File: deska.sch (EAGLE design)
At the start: 23 parts, among them Q1 BC547, X1 JST-XH-03-PIN-LONG-PAD, X2 JST-XH-03-PIN-LONG-PAD, X3 JST-XH-03-PIN-LONG-PAD, X4 JST-XH-04-PIN-LONG-PAD, X5 JST-XH-04-PIN-LONG-PAD, X6 JST-XH-04-PIN-LONG-PAD, X7 JST-XH-03-PIN-LONG-PAD

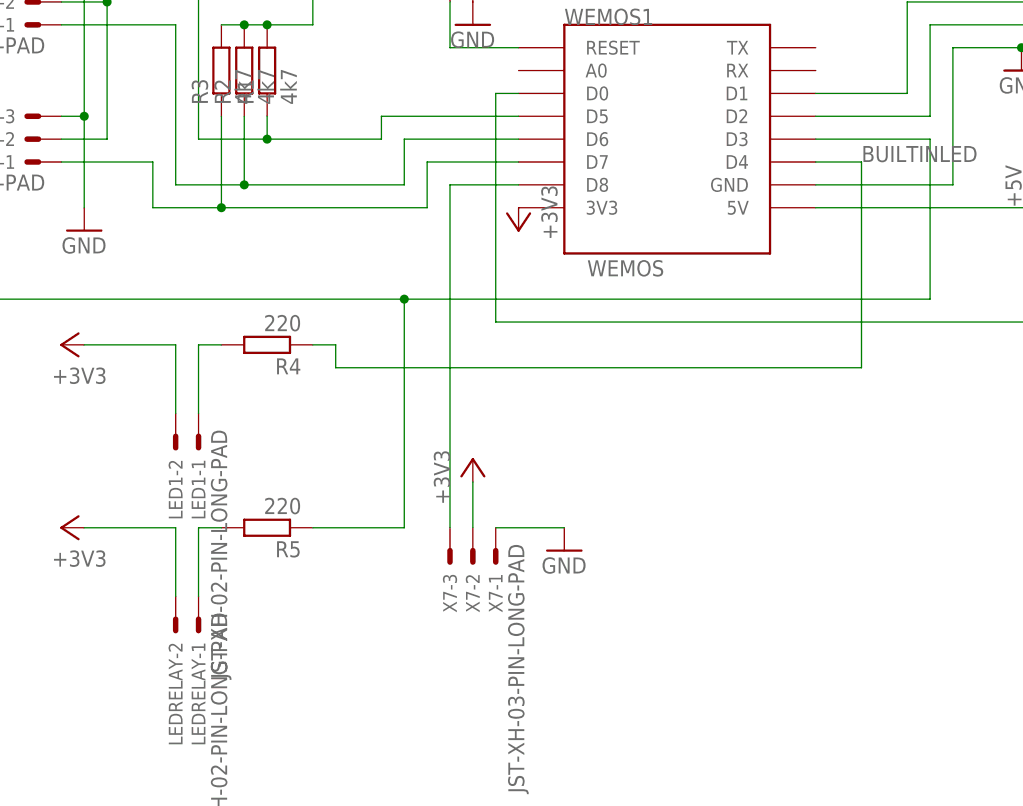
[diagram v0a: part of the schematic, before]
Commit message: deska s prohozením pinů
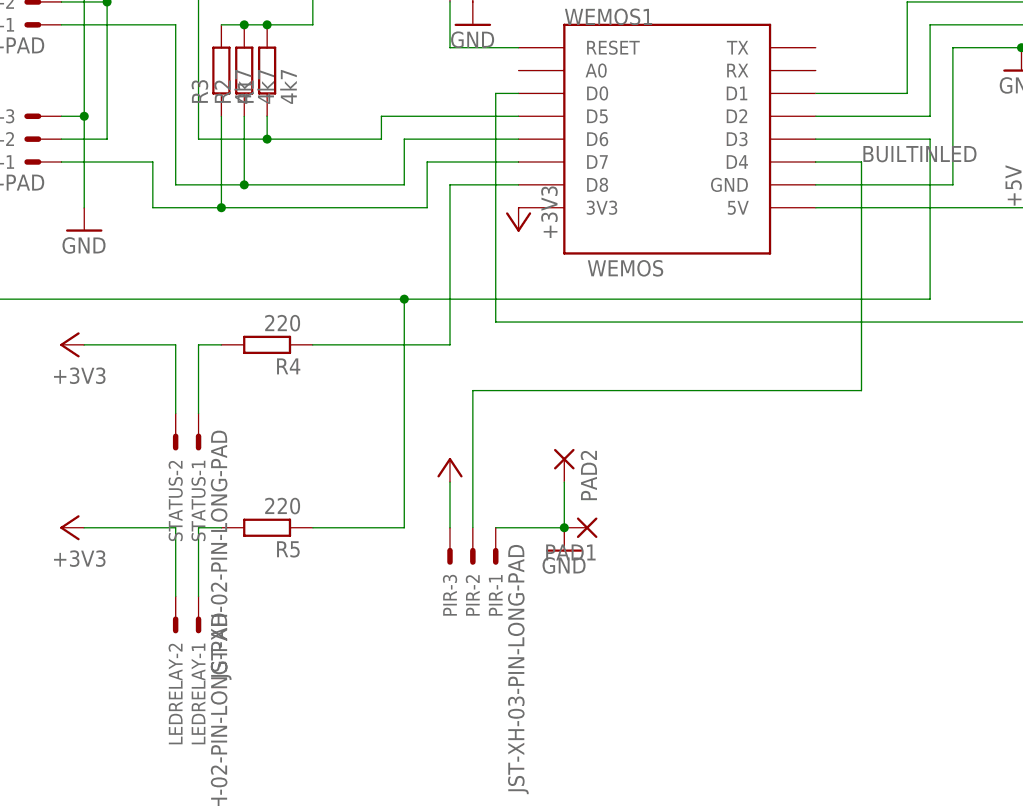
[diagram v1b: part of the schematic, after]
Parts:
- added PAD1, PAD2: (no value), wirepad:2,15/1,0
- renumbered LED1 to STATUS, X7 to PIR
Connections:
- net +3V3: now also PIR-3.S; no longer PIR-2.S
- net BUILTINLED: now also WEMOS1.D8; no longer WEMOS1.D4
- net GND: now also PAD1.P, PAD2.P
- net N$3: now also PIR-2.S, WEMOS1.D4; no longer PIR-3.S, WEMOS1.D8
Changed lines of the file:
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@@
 <part name="X6" library="Rembrandt Electronics - JST XH Connectors v1-0" deviceset="JST-XH-04-PIN" device="-LONG-PAD"/>
 <part name="RELAY" library="Rembrandt Electronics - JST XH Connectors v1-0" deviceset="JST-XH-03-PIN" device="-LONG-PAD"/>
-<part name="LED1" library="Rembrandt Electronics - JST XH Connectors v1-0" deviceset="JST-XH-02-PIN" device="-LONG-PAD"/>
+<part name="STATUS" library="Rembrandt Electronics - JST XH Connectors v1-0" deviceset="JST-XH-02-PIN" device="-LONG-PAD"/>
 <part name="LEDRELAY" library="Rembrandt Electronics - JST XH Connectors v1-0" deviceset="JST-XH-02-PIN" device="-LONG-PAD"/>
 <part name="BUZZER" library="Rembrandt Electronics - JST XH Connectors v1-0" deviceset="JST-XH-02-PIN" device="-LONG-PAD"/>
@@
 <part name="GND2" library="supply1" deviceset="GND" device=""/>
 <part name="+3V5" library="supply1" library_urn="urn:adsk.eagle:library:371" deviceset="+3V3" device=""/>
-<part name="X7" library="Rembrandt Electronics - JST XH Connectors v1-0" deviceset="JST-XH-03-PIN" device="-LONG-PAD"/>
+<part name="PIR" library="Rembrandt Electronics - JST XH Connectors v1-0" deviceset="JST-XH-03-PIN" device="-LONG-PAD"/>
 <part name="GND3" library="supply1" deviceset="GND" device=""/>
 <part name="RESET" library="Rembrandt Electronics - JST XH Connectors v1-0" deviceset="JST-XH-02-PIN" device="-LONG-PAD"/>
 <part name="GND7" library="supply1" deviceset="GND" device=""/>
+<part name="PAD1" library="wirepad" library_urn="urn:adsk.eagle:library:412" deviceset="2,15/1,0" device="" package3d_urn="urn:adsk.eagle:package:30831/1"/>
+<part name="PAD2" library="wirepad" library_urn="urn:adsk.eagle:library:412" deviceset="2,15/1,0" device="" package3d_urn="urn:adsk.eagle:package:30831/1"/>
 </parts>
 <sheets>
@@
 <attribute name="NAME" x="-33.02" y="56.642" size="1.524" layer="95" rot="R180"/>
 </instance>
-<instance part="LED1" gate="-2" x="10.16" y="27.94" smashed="yes" rot="R270">
+<instance part="STATUS" gate="-2" x="10.16" y="27.94" smashed="yes" rot="R270">
 <attribute name="NAME" x="9.398" y="25.4" size="1.524" layer="95" rot="R270"/>
 </instance>
-<instance part="LED1" gate="-1" x="12.7" y="27.94" smashed="yes" rot="R270">
+<instance part="STATUS" gate="-1" x="12.7" y="27.94" smashed="yes" rot="R270">
 <attribute name="NAME" x="11.938" y="25.4" size="1.524" layer="95" rot="R270"/>
 <attribute name="VALUE" x="14.097" y="28.702" size="1.778" layer="96" rot="R270"/>
@@
 <attribute name="VALUE" x="101.6" y="66.04" size="1.778" layer="96"/>
 </instance>
-<instance part="+3V5" gate="G$1" x="43.18" y="25.4" smashed="yes">
-<attribute name="VALUE" x="40.64" y="20.32" size="1.778" layer="96" rot="R90"/>
-</instance>
-<instance part="X7" gate="-1" x="45.72" y="15.24" smashed="yes" rot="R270">
+<instance part="+3V5" gate="G$1" x="40.64" y="25.4" smashed="yes"/>
+<instance part="PIR" gate="-1" x="45.72" y="15.24" smashed="yes" rot="R270">
 <attribute name="NAME" x="44.958" y="12.7" size="1.524" layer="95" rot="R270"/>
 <attribute name="VALUE" x="47.117" y="16.002" size="1.778" layer="96" rot="R270"/>
 </instance>
-<instance part="X7" gate="-2" x="43.18" y="15.24" smashed="yes" rot="R270">
+<instance part="PIR" gate="-2" x="43.18" y="15.24" smashed="yes" rot="R270">
 <attribute name="NAME" x="42.418" y="12.7" size="1.524" layer="95" rot="R270"/>
 </instance>
-<instance part="X7" gate="-3" x="40.64" y="15.24" smashed="yes" rot="R270">
+<instance part="PIR" gate="-3" x="40.64" y="15.24" smashed="yes" rot="R270">
 <attribute name="NAME" x="39.878" y="12.7" size="1.524" layer="95" rot="R270"/>
 </instance>
@@
 <instance part="GND7" gate="1" x="43.18" y="73.66" smashed="yes">
 <attribute name="VALUE" x="40.64" y="71.12" size="1.778" layer="96"/>
+</instance>
+<instance part="PAD1" gate="1" x="55.88" y="17.78" smashed="yes" rot="R180">
+<attribute name="NAME" x="57.023" y="15.9258" size="1.778" layer="95" rot="R180"/>
+<attribute name="VALUE" x="57.023" y="21.082" size="1.778" layer="96" rot="R180"/>
+</instance>
+<instance part="PAD2" gate="1" x="53.34" y="25.4" smashed="yes" rot="R270">
+<attribute name="NAME" x="55.1942" y="26.543" size="1.778" layer="95" rot="R270"/>
+<attribute name="VALUE" x="50.038" y="26.543" size="1.778" layer="96" rot="R270"/>
 </instance>
 </instances>
@@
 </segment>
 <segment>
-<pinref part="X7" gate="-1" pin="S"/>
 <pinref part="GND3" gate="1" pin="GND"/>
+<pinref part="PAD1" gate="1" pin="P"/>
+<pinref part="PIR" gate="-1" pin="S"/>
 <wire x1="45.72" y1="17.78" x2="53.34" y2="17.78" width="0.1524" layer="91"/>
+<junction x="53.34" y="17.78"/>
+<pinref part="PAD2" gate="1" pin="P"/>
+<wire x1="53.34" y1="22.86" x2="53.34" y2="17.78" width="0.1524" layer="91"/>
 </segment>
 <segment>
@@
 <pinref part="R4" gate="G$1" pin="2"/>
 <wire x1="12.7" y1="38.1" x2="15.24" y2="38.1" width="0.1524" layer="91"/>
-<pinref part="LED1" gate="-1" pin="S"/>
+<pinref part="STATUS" gate="-1" pin="S"/>
 <wire x1="12.7" y1="30.48" x2="12.7" y2="38.1" width="0.1524" layer="91"/>
 </segment>
@@
 <net name="BUILTINLED" class="0">
 <segment>
-<pinref part="WEMOS1" gate="D1" pin="D4"/>
-<wire x1="81.28" y1="58.42" x2="86.36" y2="58.42" width="0.1524" layer="91"/>
 <label x="86.36" y="58.42" size="1.778" layer="95"/>
-<wire x1="86.36" y1="58.42" x2="86.36" y2="35.56" width="0.1524" layer="91"/>
-<wire x1="27.94" y1="38.1" x2="25.4" y2="38.1" width="0.1524" layer="91"/>
 <pinref part="R4" gate="G$1" pin="1"/>
-<wire x1="86.36" y1="35.56" x2="27.94" y2="35.56" width="0.1524" layer="91"/>
-<wire x1="27.94" y1="35.56" x2="27.94" y2="38.1" width="0.1524" layer="91"/>
+<wire x1="25.4" y1="38.1" x2="40.64" y2="38.1" width="0.1524" layer="91"/>
+<wire x1="40.64" y1="38.1" x2="40.64" y2="55.88" width="0.1524" layer="91"/>
+<pinref part="WEMOS1" gate="D1" pin="D8"/>
+<wire x1="40.64" y1="55.88" x2="48.26" y2="55.88" width="0.1524" layer="91"/>
 </segment>
 </net>
@@
 <pinref part="+3V2" gate="G$1" pin="+3V3"/>
 <wire x1="10.16" y1="38.1" x2="0" y2="38.1" width="0.1524" layer="91"/>
-<pinref part="LED1" gate="-2" pin="S"/>
+<pinref part="STATUS" gate="-2" pin="S"/>
 <wire x1="10.16" y1="38.1" x2="10.16" y2="30.48" width="0.1524" layer="91"/>
 </segment>
@@
 </segment>
 <segment>
+<pinref part="PIR" gate="-3" pin="S"/>
 <pinref part="+3V5" gate="G$1" pin="+3V3"/>
-<wire x1="43.18" y1="22.86" x2="43.18" y2="17.78" width="0.1524" layer="91"/>
-<pinref part="X7" gate="-2" pin="S"/>
+<wire x1="40.64" y1="17.78" x2="40.64" y2="22.86" width="0.1524" layer="91"/>
 </segment>
 </net>
@@
 </segment>
 </net>
-<net name="N$3" class="0">
-<segment>
-<pinref part="WEMOS1" gate="D1" pin="D8"/>
-<wire x1="48.26" y1="55.88" x2="40.64" y2="55.88" width="0.1524" layer="91"/>
-<wire x1="40.64" y1="17.78" x2="40.64" y2="55.88" width="0.1524" layer="91"/>
-<pinref part="X7" gate="-3" pin="S"/>
-</segment>
-</net>
 <net name="N$5" class="0">
 <segment>
@@
 </segment>
 </net>
+<net name="N$3" class="0">
+<segment>
+<wire x1="43.18" y1="33.02" x2="86.36" y2="33.02" width="0.1524" layer="91"/>
+<wire x1="86.36" y1="33.02" x2="86.36" y2="58.42" width="0.1524" layer="91"/>
+<pinref part="WEMOS1" gate="D1" pin="D4"/>
+<wire x1="86.36" y1="58.42" x2="81.28" y2="58.42" width="0.1524" layer="91"/>
+<pinref part="PIR" gate="-2" pin="S"/>
+<wire x1="43.18" y1="17.78" x2="43.18" y2="33.02" width="0.1524" layer="91"/>
+</segment>
+</net>

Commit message: +
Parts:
- removed PAD1, PAD2: (no value), wirepad:2,15/1,0
- renumbered PIR to X7, STATUS to LED1
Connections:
- net +3V3: now also X7-2.S; no longer X7-3.S
- net BUILTINLED: now also WEMOS1.D4; no longer WEMOS1.D8
- net GND: no longer PAD1.P, PAD2.P
- net N$3: now also WEMOS1.D8, X7-3.S; no longer WEMOS1.D4, X7-2.S
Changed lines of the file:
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@@
 <part name="X6" library="Rembrandt Electronics - JST XH Connectors v1-0" deviceset="JST-XH-04-PIN" device="-LONG-PAD"/>
 <part name="RELAY" library="Rembrandt Electronics - JST XH Connectors v1-0" deviceset="JST-XH-03-PIN" device="-LONG-PAD"/>
-<part name="STATUS" library="Rembrandt Electronics - JST XH Connectors v1-0" deviceset="JST-XH-02-PIN" device="-LONG-PAD"/>
+<part name="LED1" library="Rembrandt Electronics - JST XH Connectors v1-0" deviceset="JST-XH-02-PIN" device="-LONG-PAD"/>
 <part name="LEDRELAY" library="Rembrandt Electronics - JST XH Connectors v1-0" deviceset="JST-XH-02-PIN" device="-LONG-PAD"/>
 <part name="BUZZER" library="Rembrandt Electronics - JST XH Connectors v1-0" deviceset="JST-XH-02-PIN" device="-LONG-PAD"/>
@@
 <part name="GND2" library="supply1" deviceset="GND" device=""/>
 <part name="+3V5" library="supply1" library_urn="urn:adsk.eagle:library:371" deviceset="+3V3" device=""/>
-<part name="PIR" library="Rembrandt Electronics - JST XH Connectors v1-0" deviceset="JST-XH-03-PIN" device="-LONG-PAD"/>
+<part name="X7" library="Rembrandt Electronics - JST XH Connectors v1-0" deviceset="JST-XH-03-PIN" device="-LONG-PAD"/>
 <part name="GND3" library="supply1" deviceset="GND" device=""/>
 <part name="RESET" library="Rembrandt Electronics - JST XH Connectors v1-0" deviceset="JST-XH-02-PIN" device="-LONG-PAD"/>
 <part name="GND7" library="supply1" deviceset="GND" device=""/>
-<part name="PAD1" library="wirepad" library_urn="urn:adsk.eagle:library:412" deviceset="2,15/1,0" device="" package3d_urn="urn:adsk.eagle:package:30831/1"/>
-<part name="PAD2" library="wirepad" library_urn="urn:adsk.eagle:library:412" deviceset="2,15/1,0" device="" package3d_urn="urn:adsk.eagle:package:30831/1"/>
 </parts>
 <sheets>
@@
 <attribute name="NAME" x="-33.02" y="56.642" size="1.524" layer="95" rot="R180"/>
 </instance>
-<instance part="STATUS" gate="-2" x="10.16" y="27.94" smashed="yes" rot="R270">
+<instance part="LED1" gate="-2" x="10.16" y="27.94" smashed="yes" rot="R270">
 <attribute name="NAME" x="9.398" y="25.4" size="1.524" layer="95" rot="R270"/>
 </instance>
-<instance part="STATUS" gate="-1" x="12.7" y="27.94" smashed="yes" rot="R270">
+<instance part="LED1" gate="-1" x="12.7" y="27.94" smashed="yes" rot="R270">
 <attribute name="NAME" x="11.938" y="25.4" size="1.524" layer="95" rot="R270"/>
 <attribute name="VALUE" x="14.097" y="28.702" size="1.778" layer="96" rot="R270"/>
@@
 <attribute name="VALUE" x="101.6" y="66.04" size="1.778" layer="96"/>
 </instance>
-<instance part="+3V5" gate="G$1" x="40.64" y="25.4" smashed="yes"/>
-<instance part="PIR" gate="-1" x="45.72" y="15.24" smashed="yes" rot="R270">
+<instance part="+3V5" gate="G$1" x="43.18" y="25.4" smashed="yes">
+<attribute name="VALUE" x="40.64" y="20.32" size="1.778" layer="96" rot="R90"/>
+</instance>
+<instance part="X7" gate="-1" x="45.72" y="15.24" smashed="yes" rot="R270">
 <attribute name="NAME" x="44.958" y="12.7" size="1.524" layer="95" rot="R270"/>
 <attribute name="VALUE" x="47.117" y="16.002" size="1.778" layer="96" rot="R270"/>
 </instance>
-<instance part="PIR" gate="-2" x="43.18" y="15.24" smashed="yes" rot="R270">
+<instance part="X7" gate="-2" x="43.18" y="15.24" smashed="yes" rot="R270">
 <attribute name="NAME" x="42.418" y="12.7" size="1.524" layer="95" rot="R270"/>
 </instance>
-<instance part="PIR" gate="-3" x="40.64" y="15.24" smashed="yes" rot="R270">
+<instance part="X7" gate="-3" x="40.64" y="15.24" smashed="yes" rot="R270">
 <attribute name="NAME" x="39.878" y="12.7" size="1.524" layer="95" rot="R270"/>
 </instance>
@@
 <instance part="GND7" gate="1" x="43.18" y="73.66" smashed="yes">
 <attribute name="VALUE" x="40.64" y="71.12" size="1.778" layer="96"/>
-</instance>
-<instance part="PAD1" gate="1" x="55.88" y="17.78" smashed="yes" rot="R180">
-<attribute name="NAME" x="57.023" y="15.9258" size="1.778" layer="95" rot="R180"/>
-<attribute name="VALUE" x="57.023" y="21.082" size="1.778" layer="96" rot="R180"/>
-</instance>
-<instance part="PAD2" gate="1" x="53.34" y="25.4" smashed="yes" rot="R270">
-<attribute name="NAME" x="55.1942" y="26.543" size="1.778" layer="95" rot="R270"/>
-<attribute name="VALUE" x="50.038" y="26.543" size="1.778" layer="96" rot="R270"/>
 </instance>
 </instances>
@@
 </segment>
 <segment>
+<pinref part="X7" gate="-1" pin="S"/>
 <pinref part="GND3" gate="1" pin="GND"/>
-<pinref part="PAD1" gate="1" pin="P"/>
-<pinref part="PIR" gate="-1" pin="S"/>
 <wire x1="45.72" y1="17.78" x2="53.34" y2="17.78" width="0.1524" layer="91"/>
-<junction x="53.34" y="17.78"/>
-<pinref part="PAD2" gate="1" pin="P"/>
-<wire x1="53.34" y1="22.86" x2="53.34" y2="17.78" width="0.1524" layer="91"/>
 </segment>
 <segment>
@@
 <pinref part="R4" gate="G$1" pin="2"/>
 <wire x1="12.7" y1="38.1" x2="15.24" y2="38.1" width="0.1524" layer="91"/>
-<pinref part="STATUS" gate="-1" pin="S"/>
+<pinref part="LED1" gate="-1" pin="S"/>
 <wire x1="12.7" y1="30.48" x2="12.7" y2="38.1" width="0.1524" layer="91"/>
 </segment>
@@
 <net name="BUILTINLED" class="0">
 <segment>
+<pinref part="WEMOS1" gate="D1" pin="D4"/>
+<wire x1="81.28" y1="58.42" x2="86.36" y2="58.42" width="0.1524" layer="91"/>
 <label x="86.36" y="58.42" size="1.778" layer="95"/>
+<wire x1="86.36" y1="58.42" x2="86.36" y2="35.56" width="0.1524" layer="91"/>
+<wire x1="27.94" y1="38.1" x2="25.4" y2="38.1" width="0.1524" layer="91"/>
 <pinref part="R4" gate="G$1" pin="1"/>
-<wire x1="25.4" y1="38.1" x2="40.64" y2="38.1" width="0.1524" layer="91"/>
-<wire x1="40.64" y1="38.1" x2="40.64" y2="55.88" width="0.1524" layer="91"/>
-<pinref part="WEMOS1" gate="D1" pin="D8"/>
-<wire x1="40.64" y1="55.88" x2="48.26" y2="55.88" width="0.1524" layer="91"/>
+<wire x1="86.36" y1="35.56" x2="27.94" y2="35.56" width="0.1524" layer="91"/>
+<wire x1="27.94" y1="35.56" x2="27.94" y2="38.1" width="0.1524" layer="91"/>
 </segment>
 </net>
@@
 <pinref part="+3V2" gate="G$1" pin="+3V3"/>
 <wire x1="10.16" y1="38.1" x2="0" y2="38.1" width="0.1524" layer="91"/>
-<pinref part="STATUS" gate="-2" pin="S"/>
+<pinref part="LED1" gate="-2" pin="S"/>
 <wire x1="10.16" y1="38.1" x2="10.16" y2="30.48" width="0.1524" layer="91"/>
 </segment>
@@
 </segment>
 <segment>
-<pinref part="PIR" gate="-3" pin="S"/>
 <pinref part="+3V5" gate="G$1" pin="+3V3"/>
-<wire x1="40.64" y1="17.78" x2="40.64" y2="22.86" width="0.1524" layer="91"/>
+<wire x1="43.18" y1="22.86" x2="43.18" y2="17.78" width="0.1524" layer="91"/>
+<pinref part="X7" gate="-2" pin="S"/>
 </segment>
 </net>
@@
 </segment>
 </net>
+<net name="N$3" class="0">
+<segment>
+<pinref part="WEMOS1" gate="D1" pin="D8"/>
+<wire x1="48.26" y1="55.88" x2="40.64" y2="55.88" width="0.1524" layer="91"/>
+<wire x1="40.64" y1="17.78" x2="40.64" y2="55.88" width="0.1524" layer="91"/>
+<pinref part="X7" gate="-3" pin="S"/>
+</segment>
+</net>
 <net name="N$5" class="0">
 <segment>
@@
 </segment>
 </net>
-<net name="N$3" class="0">
-<segment>
-<wire x1="43.18" y1="33.02" x2="86.36" y2="33.02" width="0.1524" layer="91"/>
-<wire x1="86.36" y1="33.02" x2="86.36" y2="58.42" width="0.1524" layer="91"/>
-<pinref part="WEMOS1" gate="D1" pin="D4"/>
-<wire x1="86.36" y1="58.42" x2="81.28" y2="58.42" width="0.1524" layer="91"/>
-<pinref part="PIR" gate="-2" pin="S"/>
-<wire x1="43.18" y1="17.78" x2="43.18" y2="33.02" width="0.1524" layer="91"/>
-</segment>
-</net>
